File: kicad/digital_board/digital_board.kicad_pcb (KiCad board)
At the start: 2 copper layers, 81.8 x 61.7 mm, 209 parts

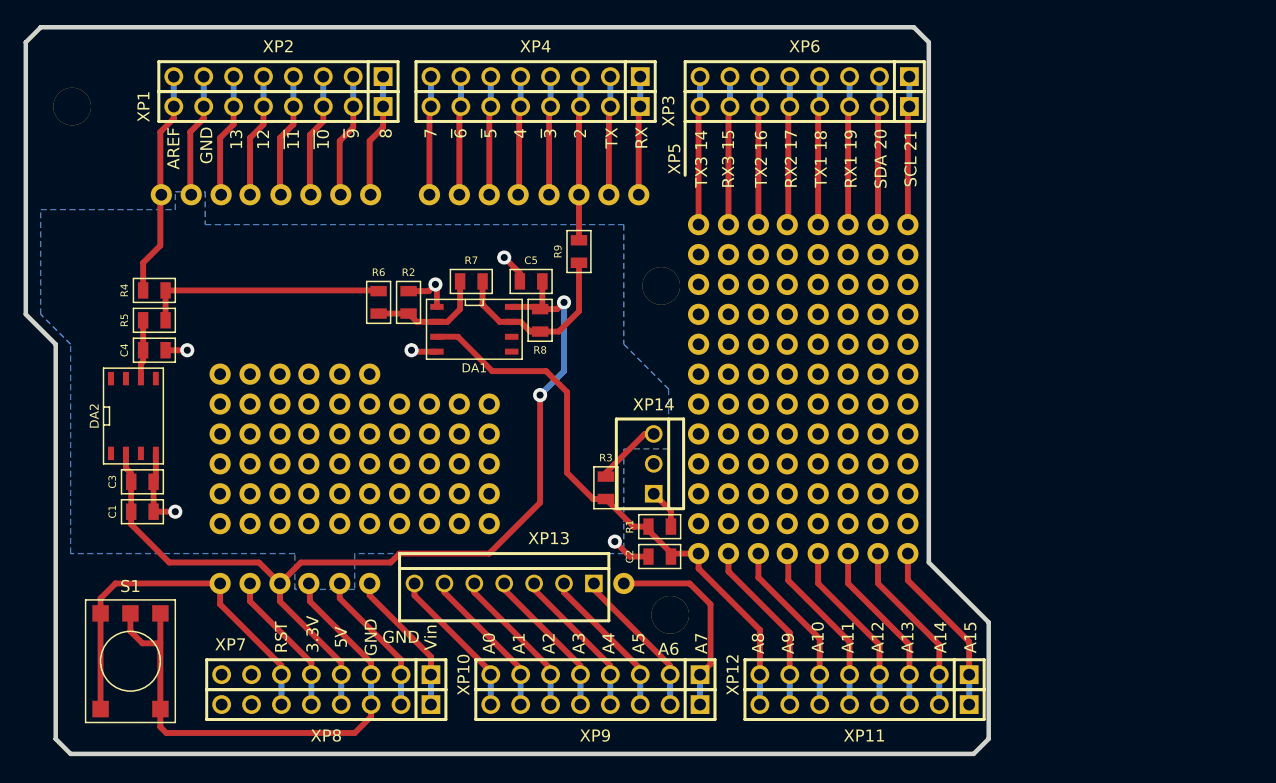
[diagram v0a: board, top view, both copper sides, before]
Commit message: Приступил к трассировке печатной платы.
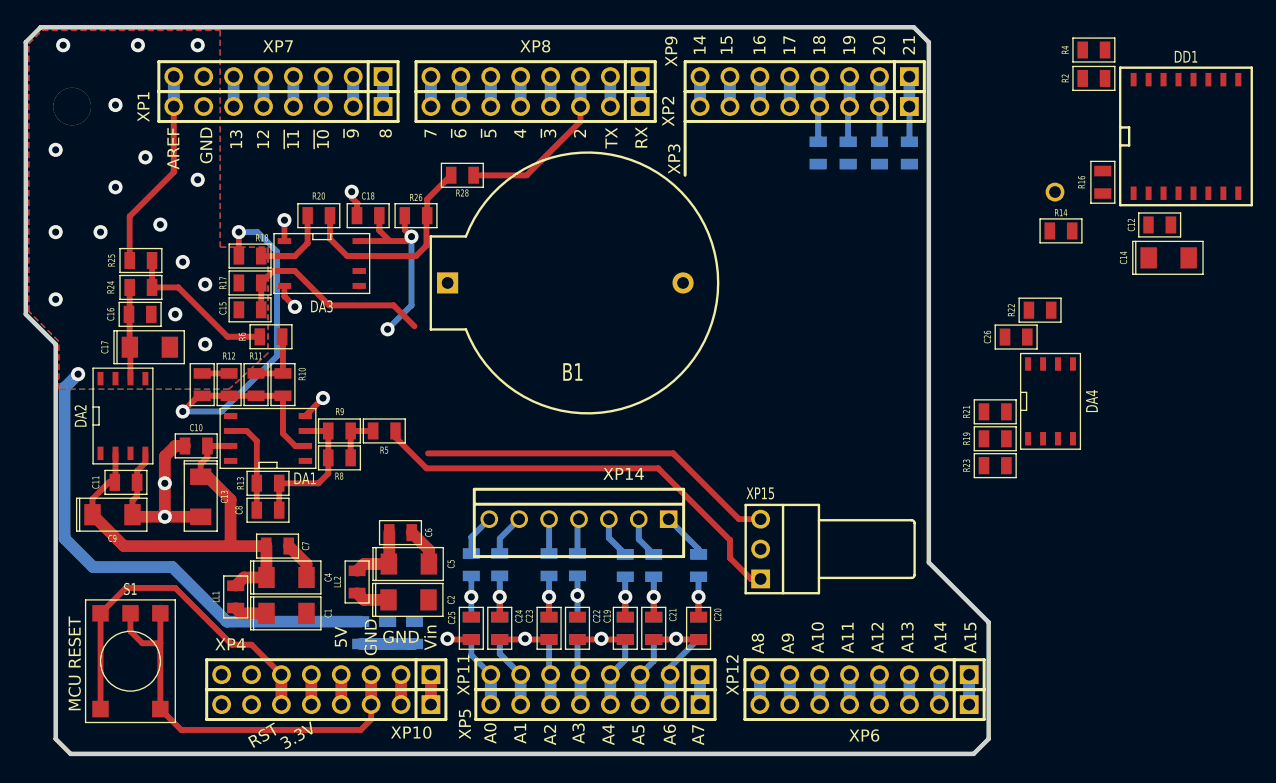
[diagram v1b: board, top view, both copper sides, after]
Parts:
- removed ? (x175): , 
- removed the arduino at (119.5, 139.8)
- removed the arduino at (119.5, 111.9)
- added B1: KLS5-CR2032-01, IWcomponents:KLS5-CR2032-01, F.Cu at (110.6, 111.6)
- added C10: 0.1 мк, IWsmd_case:SMD0805, F.Cu at (79.2, 125.5)
- added C11: 0.1 мк, IWsmd_case:SMD0805, F.Cu at (73.3, 128.6)
- added C12: 0.1 мк, IWsmd_case:SMD0805, F.Cu at (161.1, 106.7)
- added C13: 10 мк 10В, IWsmd_case:CASE_A, F.Cu at (79.6, 129.8)
- added C14: 1 мк 10В, IWsmd_case:CASE_A, F.Cu at (161.8, 109.5)
- added C15: 0.1 мк, IWsmd_case:SMD0805, F.Cu at (83.8, 113.9)
- added C16: 0.1 мк, IWsmd_case:SMD0805, F.Cu at (74.5, 114.3)
- added C17: 1 мк 10В, IWsmd_case:CASE_A, F.Cu at (75.3, 117.1)
- added C18: 0.1 мк, IWsmd_case:SMD0805, F.Cu at (93.9, 105.9)
- added C19: 1 мк, IWsmd_case:SMD0805, F.Cu at (115.7, 141.0)
- added C20: 1 мк, IWsmd_case:SMD0805, F.Cu at (121.9, 141.0)
- added C21: 1 мк, IWsmd_case:SMD0805, F.Cu at (118.1, 141.0)
- added C22: 1 мк, IWsmd_case:SMD0805, F.Cu at (111.6, 141.0)
- added C23: 1 мк, IWsmd_case:SMD0805, F.Cu at (109.2, 141.0)
- added C24: 1 мк, IWsmd_case:SMD0805, F.Cu at (105.0, 141.0)
- added C25: 1 мк, IWsmd_case:SMD0805, F.Cu at (102.6, 141.0)
- added C26: 0.1 мк, IWsmd_case:SMD0805, F.Cu at (148.9, 116.2)
- added C6: 0.1 мк, IWsmd_case:SMD0805, F.Cu at (96.6, 132.8)
- added C7: 0.1 мк, IWsmd_case:SMD0805, F.Cu at (86.2, 134.0)
- added C8: 0.001 мк, IWsmd_case:SMD0805, F.Cu at (85.3, 130.9)
- added C9: 10 мк 10В, IWsmd_case:CASE_A, F.Cu at (72.1, 131.3)
- added DA3: LM211DR, IWsmd_case:SOIC8, F.Cu at (89.9, 110.0)
- added DA4: AT24C32M/TR, IWsmd_case:SOIC8, F.Cu at (151.8, 121.7)
- added DD1: DS3231SN, IWsmd_case:SOIC16_RW16, F.Cu at (163.3, 99.2)
- added LL1: 47 мк, IWsmd_case:SMD0805, F.Cu at (82.6, 138.3)
- added LL2: 47 мк, IWsmd_case:SMD0805, F.Cu at (92.9, 137.0)
- added R10: 10 к 0.1%, IWsmd_case:SMD0805, F.Cu at (86.6, 120.3)
- added R11: NC, IWsmd_case:SMD0805, F.Cu at (84.3, 120.3)
- added R12: 10 к 0.1%, IWsmd_case:SMD0805, F.Cu at (82.0, 120.3)
- added R13: 10 к 0.1%, IWsmd_case:SMD0805, F.Cu at (85.3, 128.7)
- added R14: 4.7 к, IWsmd_case:SMD0805, F.Cu at (152.7, 107.2)
- added R15: 0, IWsmd_case:SMD0805, B.Cu at (132.1, 100.6)
- added R16: 4.7 к, IWsmd_case:SMD0805, F.Cu at (156.3, 103.1)
- added R17: 330, IWsmd_case:SMD0805, F.Cu at (83.8, 111.6)
- added R18: 0, IWsmd_case:SMD0805, F.Cu at (83.8, 109.3)
- added R19: 10 к, IWsmd_case:SMD0805, F.Cu at (147.1, 124.9)
- added R20: 100 к, IWsmd_case:SMD0805, F.Cu at (89.7, 105.9)
- added R21: 10 к, IWsmd_case:SMD0805, F.Cu at (147.1, 122.6)
- added R22: 10 к, IWsmd_case:SMD0805, F.Cu at (150.9, 113.9)
- added R23: 10 к, IWsmd_case:SMD0805, F.Cu at (147.1, 127.2)
- added R24: 0, IWsmd_case:SMD0805, F.Cu at (74.5, 112.0)
- added R25: 0, IWsmd_case:SMD0805, F.Cu at (74.5, 109.7)
- added R26: 1 к, IWsmd_case:SMD0805, F.Cu at (97.9, 105.9)
- added R27: 1 к, IWsmd_case:SMD0805, B.Cu at (115.7, 141.0)
- added R28: 0, IWsmd_case:SMD0805, F.Cu at (101.9, 102.5)
- added R29: 1 к, IWsmd_case:SMD0805, B.Cu at (115.7, 135.6)
- added R30: 1 к, IWsmd_case:SMD0805, B.Cu at (121.9, 141.0)
- added R31: 1 к, IWsmd_case:SMD0805, B.Cu at (118.1, 141.0)
- added R32: 1 к, IWsmd_case:SMD0805, B.Cu at (111.6, 141.0)
- added R33: 1 к, IWsmd_case:SMD0805, B.Cu at (109.2, 141.0)
- added R34: 1 к, IWsmd_case:SMD0805, B.Cu at (105.0, 141.0)
- added R35: 1 к, IWsmd_case:SMD0805, B.Cu at (102.6, 141.0)
- added R36: 1 к, IWsmd_case:SMD0805, B.Cu at (121.9, 135.6)
- added R37: 1 к, IWsmd_case:SMD0805, B.Cu at (118.1, 135.6)
- added R38: 1 к, IWsmd_case:SMD0805, B.Cu at (111.6, 135.6)
- added R39: 1 к, IWsmd_case:SMD0805, B.Cu at (109.2, 135.6)
- added R40: 1 к, IWsmd_case:SMD0805, B.Cu at (105.0, 135.6)
- added R41: 1 к, IWsmd_case:SMD0805, B.Cu at (102.6, 135.6)
- added R42: 0, IWsmd_case:SMD0805, B.Cu at (95.5, 141.4)
- added R43: 0, IWsmd_case:SMD0805, B.Cu at (97.8, 141.4)
- added R44: 0, IWsmd_case:SMD0805, B.Cu at (93.2, 141.4)
- added XP13: ~, IWconnectors:1_pin_1_0mm, F.Cu at (152.2, 103.9)
- C1: value 4.7 мк -> 10 мк 10В; footprint IWsmd_case:SMD0805 -> IWsmd_case:CASE_A
- C2: value 220 п -> 10 мк 10В; footprint IWsmd_case:SMD0805 -> IWsmd_case:CASE_A
- C4, C5: value 0.1 мк -> 10 мк 10В; footprint IWsmd_case:SMD0805 -> IWsmd_case:CASE_A
- DA1: value LM211DR -> ADA4522-1ARZ
- DA2: value REF198ESZ -> ADR444BRZ
- R1: value 220 -> 0; moved to B.Cu
- R2: value 10 к -> 4.7 к
- R3: value 47 к -> 0; moved to B.Cu
- R4: value 0 -> 4.7 к
- R5, R9: value 0 -> 10 к 0.1%
- R6: value 10 к -> 10 к 0.1%
- R7: value 100 к -> 0; moved to B.Cu
- R8: value 1 к -> NC
- XP15: renamed from XP14; value WF-3 -> WF-3R; footprint IWconnectors:WF-3 -> IWconnectors:WF-3R
- moved R4 82.4 mm to (155.5, 91.8), turned to 0 degrees
- moved R2 61.2 mm to (155.5, 94.3), turned to 0 degrees
- moved R7 38.8 mm to (139.8, 100.6), turned to 90 degrees
- moved R3 36.7 mm to (137.3, 100.6)
- moved R1 35.6 mm to (134.6, 100.6), turned to 90 degrees
- moved C5 26.2 mm to (97.3, 135.5), turned to 0 degrees
- moved R9 25.4 mm to (91.4, 124.2), turned to 0 degrees
- moved C4 22.3 mm to (86.9, 136.7)
- moved R5 21.7 mm to (95.2, 124.2), turned to 0 degrees
- moved C2 21.7 mm to (97.3, 138.6), turned to 0 degrees
- moved R8 20.7 mm to (91.4, 126.5), turned to 0 degrees
- moved DA1 19.8 mm to (85.3, 124.8), turned to 90 degrees
- moved C1 15.0 mm to (86.9, 139.7)
- moved XP15 11.6 mm to (127.2, 134.2), turned to -90 degrees
- moved C3 9.69 mm to (79.8, 120.3), turned to 90 degrees
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- renumbered XP8 to XP10, XP10 to XP11, XP13 to XP14, XP3 to XP2, XP5 to XP3, XP7 to XP4, XP9 to XP5, XP11 to XP6, XP2 to XP7, XP4 to XP8, XP6 to XP9
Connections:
- C2 pad 1: /ADC8 -> /VCC
- C3 pad 1: /VCC -> Net-(DA1-~{IN1})
- C3 pad 2: /GND -> /SGND
- C4 pad 1: /VREF -> /5VA
- C4 pad 2: /GND -> /AGND
- C5 pad 1: /VCC -> /5VD
- C5 pad 2: /GND -> /DGND
- DA1 pad 1: /GND -> unconnected-(DA1-NC-Pad1)
- DA1 pad 2: Net-(DA1-Pad2) -> Net-(DA1-~{IN1})
- DA1 pad 3: /ADC8 -> Net-(DA1-IN1)
- DA1 pad 4: /GND -> /AGND
- DA1 pad 5: Net-(DA1-Pad5) -> (no net)
- DA1 pad 7: /CMP_OUT -> /5VA
- DA1 pad 8: /VCC -> unconnected-(DA1-NC-Pad8)
- DA2 pad 1: Net-(DA2-Pad1) -> unconnected-(DA2-TP-Pad1)
- DA2 pad 2: /VCC -> /5VA
- DA2 pad 3: Net-(DA2-Pad3) -> unconnected-(DA2-NC-Pad3)
- DA2 pad 4: /GND -> /AGND
- DA2 pad 5: Net-(DA2-Pad5) -> unconnected-(DA2-TRIM-Pad5)
- DA2 pad 6: /VREF -> Net-(DA2-Vout)
- DA2 pad 7: Net-(DA2-Pad7) -> unconnected-(DA2-NC-Pad7)
- DA2 pad 8: Net-(DA2-Pad8) -> unconnected-(DA2-TP-Pad8)
- R1 pad 1: /ADC8 -> /RTC_RST
- R1 pad 2: /SIG_IN -> /PD2
- R2 pad 1: Net-(DA1-Pad2) -> /5VD
- R2 pad 2: /GND -> /SCL
- R3 pad 1: /ADC8 -> /SDA
- R3 pad 2: /GND -> /PD1
- R4 pad 1: Net-(R4-Pad1) -> /5VD
- R4 pad 2: /AREF -> /SDA
- R5 pad 1: Net-(R4-Pad1) -> Net-(R5-Pad1)
- R5 pad 2: /VREF -> /SIG_IN
- R6 pad 1: Net-(R4-Pad1) -> Net-(R10-Pad2)
- R6 pad 2: Net-(DA1-Pad2) -> /VREF
- R7 pad 1: /CMP_OUT -> /SCL
- R7 pad 2: Net-(DA1-Pad2) -> /PD0
- R8 pad 1: /VCC -> Net-(DA1-IN1)
- R8 pad 2: /CMP_OUT -> Net-(R5-Pad1)
- R9 pad 1: /PE4 -> Net-(DA1-IN1)
- R9 pad 2: /CMP_OUT -> Net-(R5-Pad1)
- S1 pad 5: /GND -> (no net)
- XP1 pad 7: /GND -> unconnected-(XP1-Pad7)
- XP10 pad 7: Net-(XP8-Pad7) -> unconnected-(XP10-Pad7)
- XP10 pad 8: Net-(XP8-Pad8) -> unconnected-(XP10-Pad8)
- XP14 pad 1: /ADC6 -> Net-(R36-Pad1)
- XP14 pad 2: /ADC5 -> Net-(R37-Pad1)
- XP14 pad 3: /ADC4 -> Net-(R29-Pad1)
- XP14 pad 4: /ADC3 -> Net-(R38-Pad1)
- XP14 pad 5: /ADC2 -> Net-(R39-Pad1)
- XP14 pad 6: /ADC1 -> Net-(R40-Pad1)
- XP14 pad 7: /ADC0 -> Net-(R41-Pad1)
- XP15 pad 2: Net-(XP14-Pad2) -> unconnected-(XP15-Pad2)
- XP15 pad 3: /GND -> /SGND
- XP4 pad 7: Net-(XP7-Pad7) -> unconnected-(XP4-Pad7)
- XP4 pad 8: Net-(XP7-Pad8) -> unconnected-(XP4-Pad8)
- XP7 pad 7: /GND -> unconnected-(XP7-Pad7)
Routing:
- net /VCC: track 83.9 -> 8.25 mm, vias 2 -> 0
- net /SGND: track 0.00 -> 75.4 mm, vias 0 -> 17
- net /GND: track 96.4 -> 42.0 mm, vias 6 -> 0
- net /5VA: track 0.00 -> 39.8 mm
- net Net-(DA1-~{IN1}): track 0.00 -> 39.4 mm, vias 0 -> 2
- net /SIG_IN: track 3.40 -> 37.4 mm
- net /ADC8: track 49.4 -> 20.2 mm
- net /AGND: track 0.00 -> 24.5 mm, vias 0 -> 3
- net /DGND: track 0.00 -> 23.7 mm, vias 0 -> 7
- net /5VD: track 0.00 -> 23.5 mm, vias 0 -> 2
- net Net-(R4-Pad1): track 20.6 -> 0.00 mm
- net /ADC7: track 17.0 -> 2.54 mm
- net /ADC15: track 15.0 -> 2.54 mm
- net /ADC11: track 15.0 -> 2.54 mm
- net /ADC9: track 15.0 -> 2.54 mm
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- added copper zone on B.Cu, net /SGND
- added copper zone on F.Cu, net /SGND
- removed copper zone on B.Cu, net /GND
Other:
- board text added: "14"
- board text added: "15"
- board text added: "16"
- board text added: "17"
- board text added: "18"
- board text added: "19"
- board text added: "20"
- board text added: "21"
- board text added: "MCU RESET"
- board text removed: "RX1 19"
- board text removed: "RX2 17"
- board text removed: "RX3 15"
- board text removed: "SCL 21"
- board text removed: "SDA 20"
- board text removed: "TX1 18"
- board text removed: "TX2 16"
- board text removed: "TX3 14"

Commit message: Закончил трассировку цифровой печатной платы.
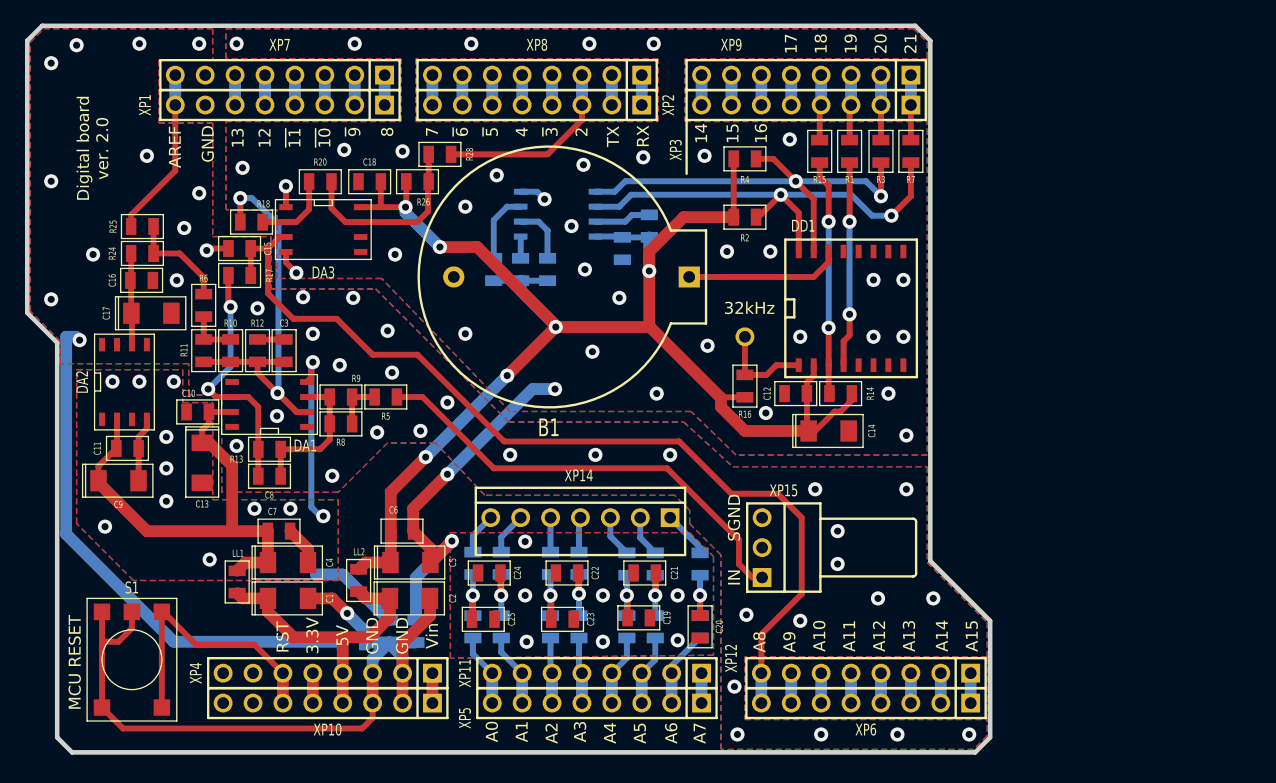
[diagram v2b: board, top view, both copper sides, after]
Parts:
- removed arduino: P***, 1_pin
- C26, DA4, R19, R21, R22, R23: moved to B.Cu
- R1, R15, R3, R7: moved to F.Cu
- moved R23 45.7 mm to (104.5, 110.5), turned to -90 degrees
- moved DA4 44.8 mm to (110.0, 105.8), turned to 90 degrees
- moved R19 42.8 mm to (106.8, 110.5), turned to -90 degrees
- moved R21 39.9 mm to (109.1, 110.5), turned to -90 degrees
- moved R16 35.0 mm to (125.9, 120.4), turned to 90 degrees
- moved C26 34.3 mm to (115.4, 108.7), turned to -90 degrees
- moved C12 34.1 mm to (130.2, 121.0), turned to 180 degrees
- moved R22 34.0 mm to (117.7, 106.8), turned to -90 degrees
- moved C14 32.4 mm to (133.0, 124.2)
- moved DD1 32.0 mm to (134.9, 113.8)
- moved R2 31.9 mm to (125.9, 106.0)
- moved R4 31.1 mm to (125.9, 101.1)
- moved XP13 29.1 mm to (125.9, 116.2)
- moved R14 23.3 mm to (134.0, 121.0), turned to 180 degrees
- moved C3 7.53 mm to (86.7, 117.4)
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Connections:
- S1 pad 1: /RESET -> /GND
- S1 pad 2: /RESET -> /GND
- S1 pad 3: /GND -> /RESET
- S1 pad 4: /GND -> /RESET
- S1 pad 5: (no net) -> /GND
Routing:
- net /5VD: track 23.5 -> 130.0 mm, vias 2 -> 6
- net /ADC8: track 20.2 -> 79.9 mm
- net /SCL: track 0.00 -> 39.8 mm, vias 0 -> 2
- net /SDA: track 0.00 -> 38.8 mm, vias 0 -> 2
- net /SGND: track 75.4 -> 49.8 mm, vias 17 -> 42
- net /GND: track 42.0 -> 67.3 mm, vias 0 -> 1
- net /SQW: track 0.00 -> 20.0 mm, vias 0 -> 2
- net /VCC: track 8.25 -> 26.0 mm
- net /RTC_RST: track 0.00 -> 17.4 mm, vias 0 -> 2
- net /DGND: track 23.7 -> 38.2 mm, vias 7 -> 45
- net Net-(DD1-Vbat): track 0.00 -> 13.3 mm
- net Net-(DA1-OUT): track 8.46 -> 21.6 mm, vias 0 -> 2
- net Net-(DD1-32kHz): track 0.00 -> 8.16 mm
- net /AGND: track 24.5 -> 32.2 mm, vias 3 -> 12
- net /RESET: track 29.5 -> 23.1 mm
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- added copper zone on B.Cu, net /AGND
- added copper zone on F.Cu, net /AGND
- added copper zone on B.Cu, net /DGND
- added copper zone on F.Cu, net /DGND
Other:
- rule pad_to_mask_clearance: 0.254 -> 0.2
- board text added: "32kHz"
- board text added: "Digital board ver. 2.0"
- board text added: "IN"
- board text added: "SGND"

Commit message: Отправил печатные платы digital_board в производство.
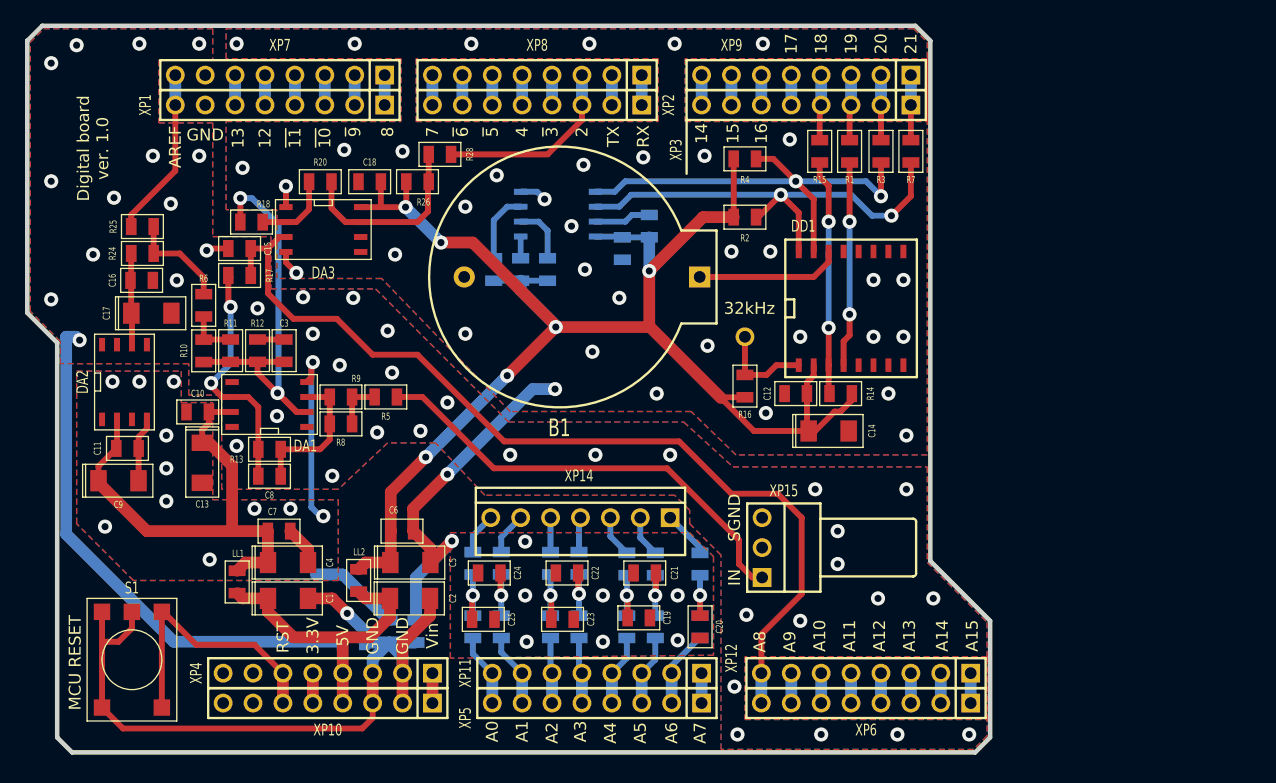
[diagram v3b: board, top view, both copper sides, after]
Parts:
- moved R10 2.29 mm to (79.9, 117.4)
- moved R11 2.29 mm to (82.2, 117.4)
- moved B1 0.89 mm to (112.0, 111.1)
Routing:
- net /5VD: track 130.0 -> 128.4 mm
- net Net-(DD1-Vbat): track 13.3 -> 12.4 mm
- net Net-(DA1-OUT): track 21.6 -> 21.0 mm
- net /SGND: vias 42 -> 43
- net /DGND: vias 45 -> 46
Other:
- board text added: "Digital board ver. 1.0"
- board text removed: "Digital board ver. 2.0"

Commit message: Исправил ошибки в схеме и на печатной плате. Увеличил версию цифровой платы до 1.1.
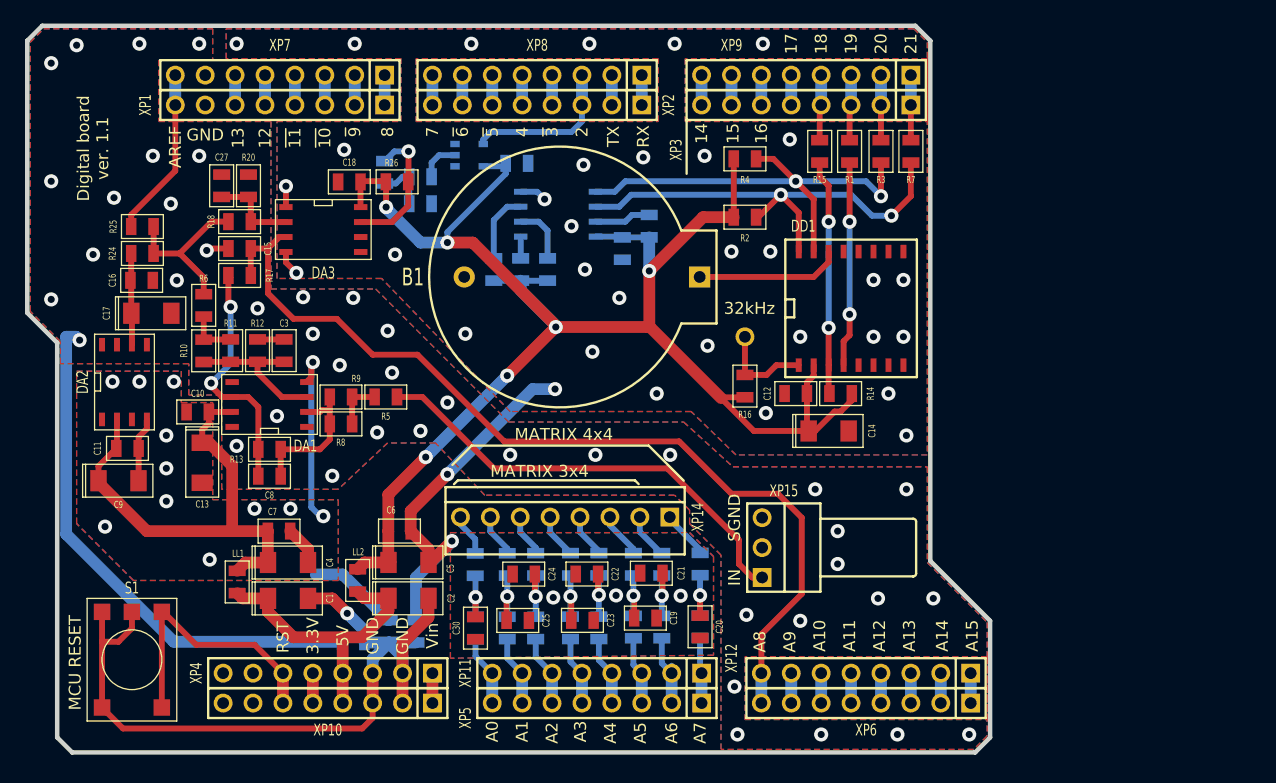
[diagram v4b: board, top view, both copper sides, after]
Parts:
- added C27: 0.1 мк, IWsmd_case:SMD0805, F.Cu at (81.4, 103.4)
- added C28: 0.1 мк, IWsmd_case:SMD0805, B.Cu at (98.3, 104.9)
- added C29: 0.1 мк, IWsmd_case:SMD0805, B.Cu at (106.5, 101.5)
- added C30: 100 п*, IWsmd_case:SMD0805, F.Cu at (103.0, 141.0)
- added DD3: SN74LVC1G17DBVR, IWsmd_case:SOT753, B.Cu at (102.4, 100.8)
- added R45: 10 к, IWsmd_case:SMD0805, B.Cu at (98.3, 102.6)
- added R46: 1 к*, IWsmd_case:SMD0805, B.Cu at (103.0, 140.9)
- added R47: 1 к*, IWsmd_case:SMD0805, B.Cu at (102.9, 135.6)
- C19, C20, C21, C22, C23, C24, C25: value 1 мк -> 100 п*
- C8: value 0.001 мк -> 1 н
- R18: value 0 -> 100 к 0.1%
- R20: value 100 к -> 100 к 0.1%
- R27, R29, R30, R31, R32, R33, R34, R35, R36, R37, R38, R39, R40, R41: value 1 к -> 1 к*
- R28: value 0 -> 10 к; moved to B.Cu
- XP14: value WF-7 -> WF-8; footprint IWconnectors:WF-7 -> IWconnectors:WF-8
- moved R20 6.11 mm to (83.7, 103.4), turned to 90 degrees
- moved R28 4.94 mm to (95.2, 102.2), turned to 90 degrees
- moved C24 2.93 mm to (107.1, 136.4)
- moved R35 2.93 mm to (105.7, 140.9)
- moved R41 2.93 mm to (105.7, 135.5)
- moved C25 2.93 mm to (106.6, 140.3)
- moved R34 2.93 mm to (108.1, 140.9)
- moved R40 2.93 mm to (108.1, 135.5)
- moved R26 1.74 mm to (96.3, 103.0)
- moved C18 1.73 mm to (92.3, 103.0)
- moved R33 1.69 mm to (111.0, 140.9)
- moved R39 1.69 mm to (111.0, 135.5)
- moved C22 1.69 mm to (112.4, 136.4)
- moved C23 1.69 mm to (112.1, 140.3)
- moved R32 1.69 mm to (113.5, 140.9)
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- renumbered DA4 to DD2
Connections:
- C3 pad 1: Net-(DA1-~{IN1}) -> Net-(DA1-IN1)
- C8 pad 1: Net-(DA1-IN1) -> Net-(DA1-~{IN1})
- R10 pad 1: Net-(DA1-~{IN1}) -> Net-(DA1-IN1)
- R11 pad 1: Net-(DA1-~{IN1}) -> Net-(DA1-IN1)
- R12 pad 1: Net-(DA1-~{IN1}) -> Net-(DA1-IN1)
- R13 pad 2: Net-(DA1-IN1) -> Net-(DA1-~{IN1})
- R18 pad 1: Net-(DA3-IN+) -> /VREF
- R18 pad 2: Net-(DA1-~{IN1}) -> Net-(DA3-IN+)
- R20 pad 1: /CMP_OUT -> Net-(DA3-IN+)
- R20 pad 2: Net-(DA3-IN+) -> /SGND
- R27 pad 2: /ADC4 -> /ADC5
- R28 pad 1: /PE4 -> Net-(C28-Pad1)
- R30 pad 2: /ADC6 -> /ADC7
- R31 pad 2: /ADC5 -> /ADC6
- R32 pad 2: /ADC3 -> /ADC4
- R33 pad 2: /ADC2 -> /ADC3
- R34 pad 2: /ADC1 -> /ADC2
- R35 pad 2: /ADC0 -> /ADC1
- R8 pad 1: Net-(DA1-IN1) -> Net-(DA1-~{IN1})
- R9 pad 1: Net-(DA1-IN1) -> Net-(DA1-~{IN1})
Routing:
- net Net-(DA1-~{IN1}): track 35.4 -> 12.4 mm, vias 2 -> 0
- net /5VD: track 128.4 -> 139.4 mm
- net /VREF: track 8.81 -> 14.1 mm
- net Net-(C30-Pad1): track 0.00 -> 5.17 mm, vias 0 -> 1
- net Net-(C28-Pad1): track 0.00 -> 4.62 mm
- net /CMP_OUT: track 16.2 -> 11.6 mm, vias 0 -> 1
- net Net-(R47-Pad1): track 0.00 -> 3.61 mm
- net Net-(DD3-IN_A): track 0.00 -> 3.45 mm
- net /ADC7: track 2.54 -> 5.64 mm
- net /PE4: track 16.1 -> 13.3 mm
- net Net-(R39-Pad1): track 2.93 -> 3.78 mm
- net Net-(R38-Pad1): track 2.97 -> 3.72 mm
- net Net-(DA3-IN+): track 6.74 -> 7.46 mm
- net /DGND: track 38.2 -> 38.5 mm, vias 46 -> 38
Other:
- board text added: "Digital board ver. 1.1"
- board text added: "MATRIX 3x4"
- board text added: "MATRIX 4x4"
- board text removed: "Digital board ver. 1.0"
